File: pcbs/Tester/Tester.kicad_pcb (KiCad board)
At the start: 2 copper layers, 106 parts, among them J201 Raspberry_Pi_2_3, J301 Conn_02x20_Odd_Even, J401 Conn_02x20_Odd_Even, U201 SN74LVC4245APWR, U202 SN74LVC4245APWR, U203 SN74LVC4245APWR, U301 74HC595, U302 74HC595, U303 74HC595, U304 74HC595, U305 74HC595, U401 74HC165, U402 74HC165, U403 74HC165, U404 74HC165, U405 74HC165

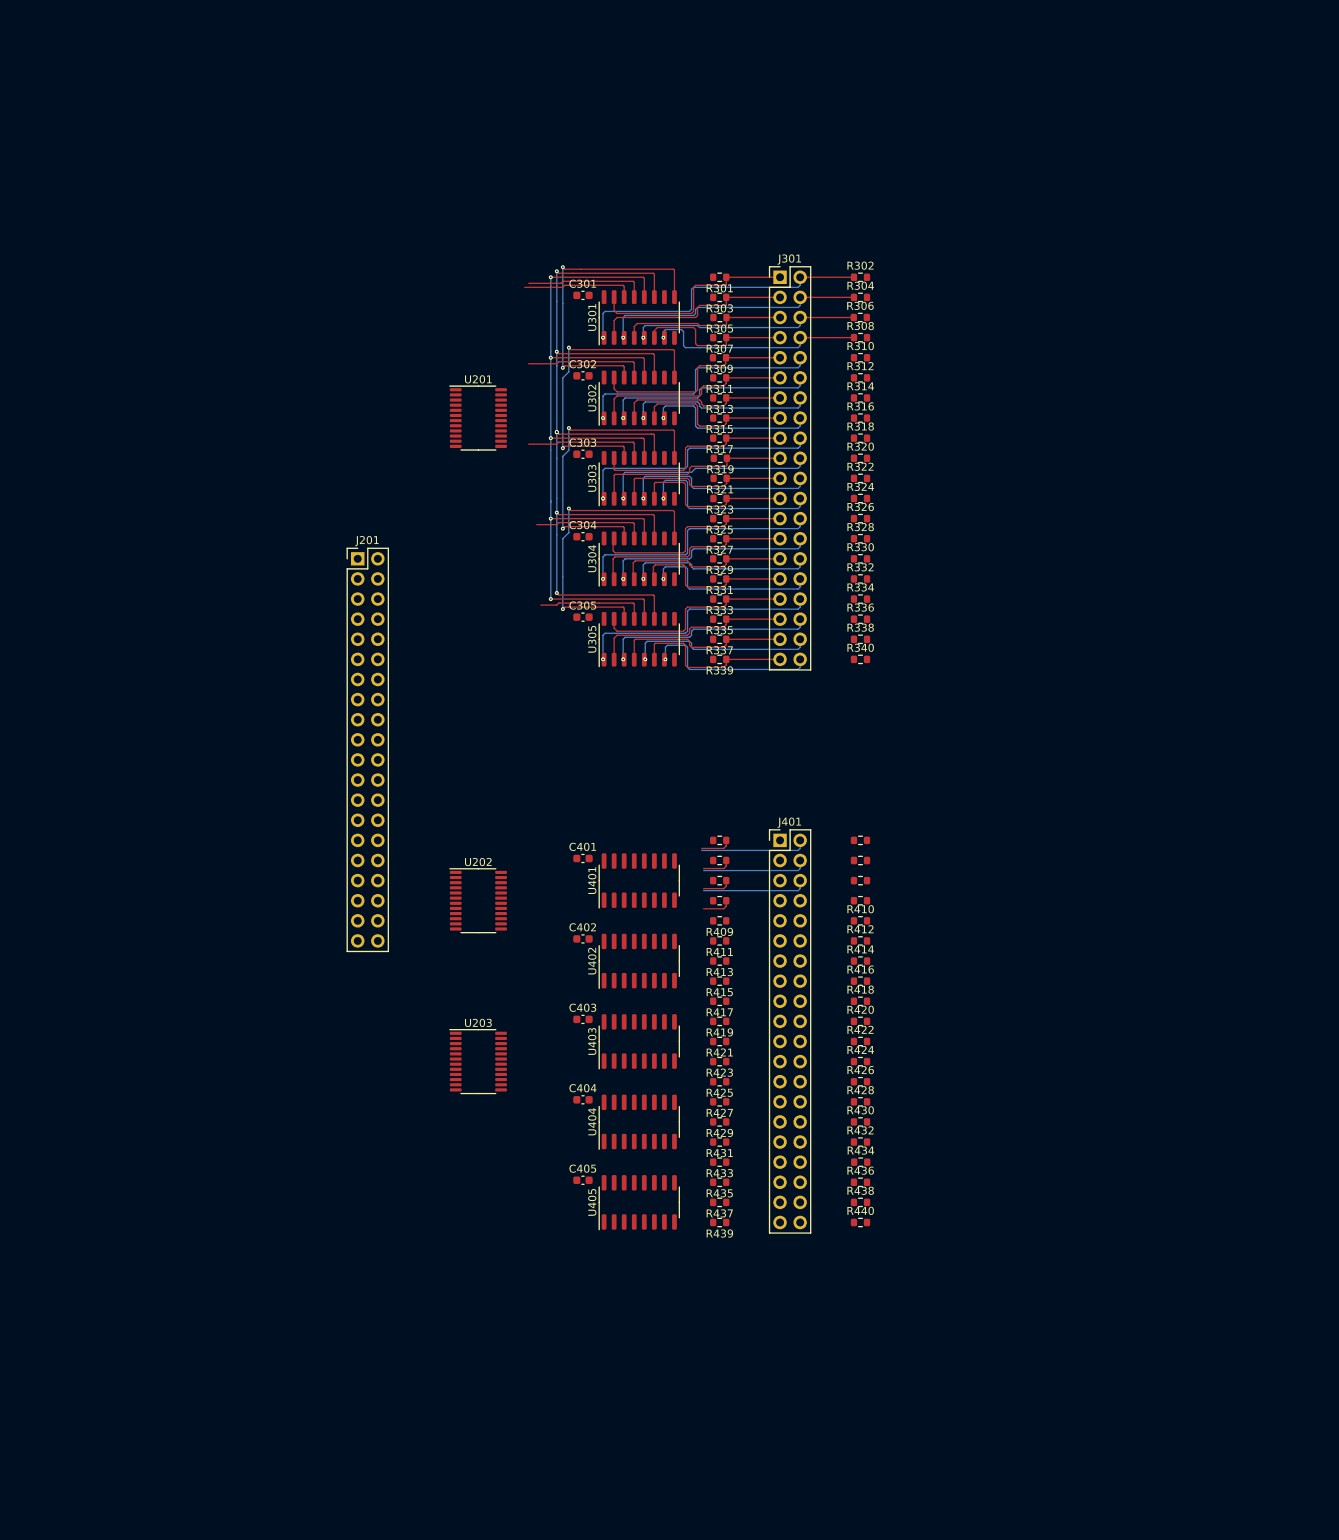
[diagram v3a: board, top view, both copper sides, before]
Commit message: Shift register routing
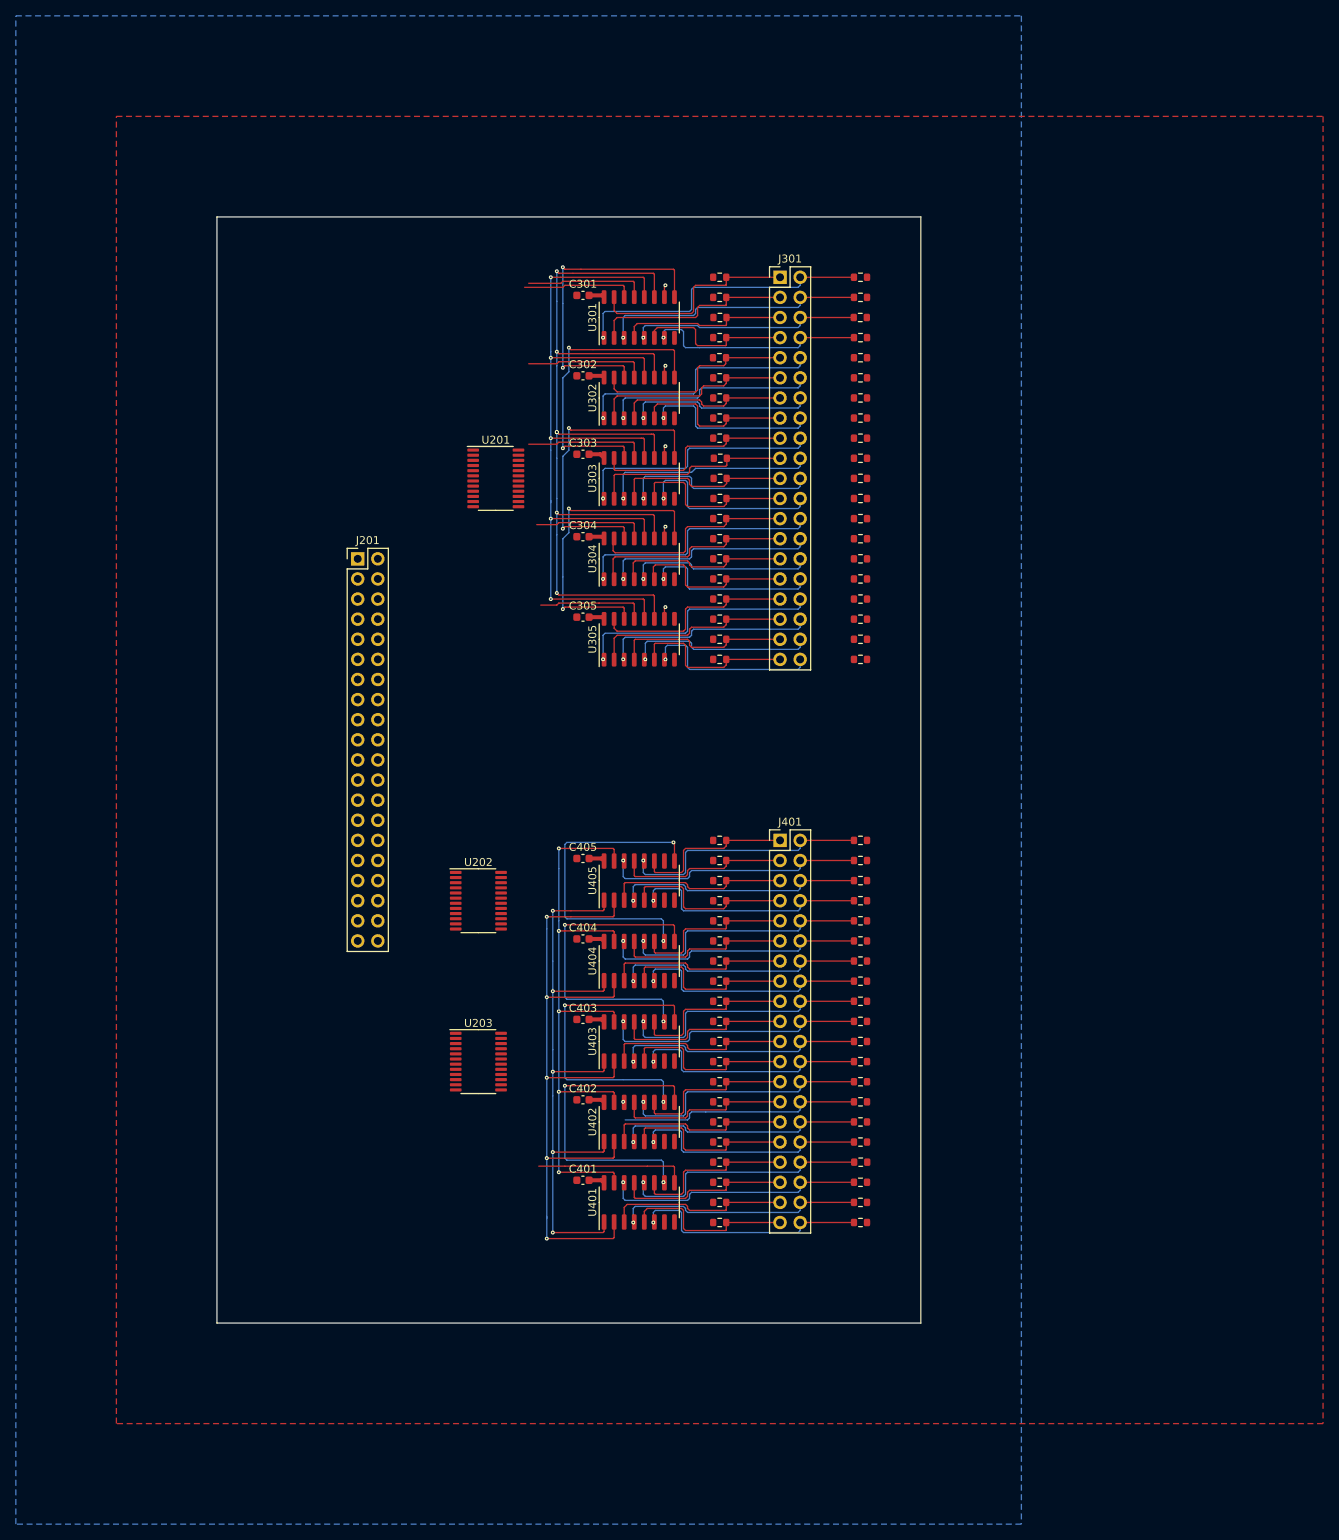
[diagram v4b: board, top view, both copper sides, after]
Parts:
- moved U401 40.6 mm to (129.5, 149.9)
- moved U405 40.6 mm to (129.5, 109.2)
- moved C401 40.6 mm to (122.4, 147.1)
- moved C405 40.6 mm to (122.4, 106.4)
- moved C402 20.3 mm to (122.4, 136.9)
- moved C404 20.3 mm to (122.4, 116.6)
- moved U402 20.3 mm to (129.5, 139.7)
- moved U404 20.3 mm to (129.5, 119.4)
- moved U201 7.93 mm to (111.4, 58.4)
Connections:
- U401 pad 11: /In Registers/In_{7} -> /In Registers/In_{32}
- U401 pad 12: /In Registers/In_{6} -> /In Registers/In_{33}
- U401 pad 13: /In Registers/In_{5} -> /In Registers/In_{34}
- U401 pad 14: /In Registers/In_{4} -> /In Registers/In_{35}
- U401 pad 3: /In Registers/In_{3} -> /In Registers/In_{36}
- U401 pad 4: /In Registers/In_{2} -> /In Registers/In_{37}
- U401 pad 5: /In Registers/In_{1} -> /In Registers/In_{38}
- U401 pad 6: /In Registers/In_{0} -> /In Registers/In_{39}
- U402 pad 11: unconnected-(U402-Pad11) -> /In Registers/In_{24}
- U402 pad 12: unconnected-(U402-Pad12) -> /In Registers/In_{25}
- U402 pad 13: unconnected-(U402-Pad13) -> /In Registers/In_{26}
- U402 pad 14: unconnected-(U402-Pad14) -> /In Registers/In_{27}
- U402 pad 3: unconnected-(U402-Pad3) -> /In Registers/In_{28}
- U402 pad 4: unconnected-(U402-Pad4) -> /In Registers/In_{29}
- U402 pad 5: unconnected-(U402-Pad5) -> /In Registers/In_{30}
- U402 pad 6: unconnected-(U402-Pad6) -> /In Registers/In_{31}
- U403 pad 11: unconnected-(U403-Pad11) -> /In Registers/In_{16}
- U403 pad 12: unconnected-(U403-Pad12) -> /In Registers/In_{17}
- U403 pad 13: unconnected-(U403-Pad13) -> /In Registers/In_{18}
- U403 pad 14: unconnected-(U403-Pad14) -> /In Registers/In_{19}
- U403 pad 3: unconnected-(U403-Pad3) -> /In Registers/In_{20}
- U403 pad 4: unconnected-(U403-Pad4) -> /In Registers/In_{21}
- U403 pad 5: unconnected-(U403-Pad5) -> /In Registers/In_{22}
- U403 pad 6: unconnected-(U403-Pad6) -> /In Registers/In_{23}
- U404 pad 11: unconnected-(U404-Pad11) -> /In Registers/In_{8}
- U404 pad 12: unconnected-(U404-Pad12) -> /In Registers/In_{9}
- U404 pad 13: unconnected-(U404-Pad13) -> /In Registers/In_{10}
- U404 pad 14: unconnected-(U404-Pad14) -> /In Registers/In_{11}
- U404 pad 3: unconnected-(U404-Pad3) -> /In Registers/In_{12}
- U404 pad 4: unconnected-(U404-Pad4) -> /In Registers/In_{13}
- U404 pad 5: unconnected-(U404-Pad5) -> /In Registers/In_{14}
- U404 pad 6: unconnected-(U404-Pad6) -> /In Registers/In_{15}
- U405 pad 11: unconnected-(U405-Pad11) -> /In Registers/In_{0}
- U405 pad 12: unconnected-(U405-Pad12) -> /In Registers/In_{1}
- U405 pad 13: unconnected-(U405-Pad13) -> /In Registers/In_{2}
- U405 pad 14: unconnected-(U405-Pad14) -> /In Registers/In_{3}
- U405 pad 3: unconnected-(U405-Pad3) -> /In Registers/In_{4}
- U405 pad 4: unconnected-(U405-Pad4) -> /In Registers/In_{5}
- U405 pad 5: unconnected-(U405-Pad5) -> /In Registers/In_{6}
- U405 pad 6: unconnected-(U405-Pad6) -> /In Registers/In_{7}
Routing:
- net /In Registers/IN_{CLK}: track 0.00 -> 93.6 mm, vias 0 -> 5
- net /In Registers/~{IN_{SELECT}}: track 0.00 -> 82.1 mm, vias 0 -> 5
- net /In Registers/~{IN_{LOAD}}: track 0.00 -> 79.3 mm, vias 0 -> 5
- net Net-(U404-Pad10): track 0.00 -> 40.6 mm, vias 0 -> 2
- net Net-(U401-Pad10): track 0.00 -> 40.2 mm, vias 0 -> 2
- net Net-(U403-Pad10): track 0.00 -> 40.2 mm, vias 0 -> 2
- net Net-(U402-Pad10): track 0.00 -> 40.2 mm, vias 0 -> 2
- net /In Registers/In_{19}: track 0.00 -> 33.6 mm, vias 0 -> 1
- net /In Registers/In_{35}: track 0.00 -> 33.1 mm, vias 0 -> 1
- net /In Registers/In_{11}: track 0.00 -> 33.1 mm, vias 0 -> 1
- net /In Registers/In_{17}: track 0.00 -> 32.6 mm, vias 0 -> 1
- net /In Registers/In_{33}: track 0.00 -> 32.1 mm, vias 0 -> 1
- net /In Registers/In_{9}: track 0.00 -> 32.1 mm, vias 0 -> 1
- net /In Registers/In_{25}: track 0.00 -> 32.1 mm, vias 0 -> 1
- net /In Registers/In_{29}: track 0.00 -> 31.3 mm, vias 0 -> 1
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- added copper zone on B.Cu, net +5V
- added copper zone on F.Cu, net /In Registers/In_{3}
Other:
- board outline added: 88.9 x 139.7 mm

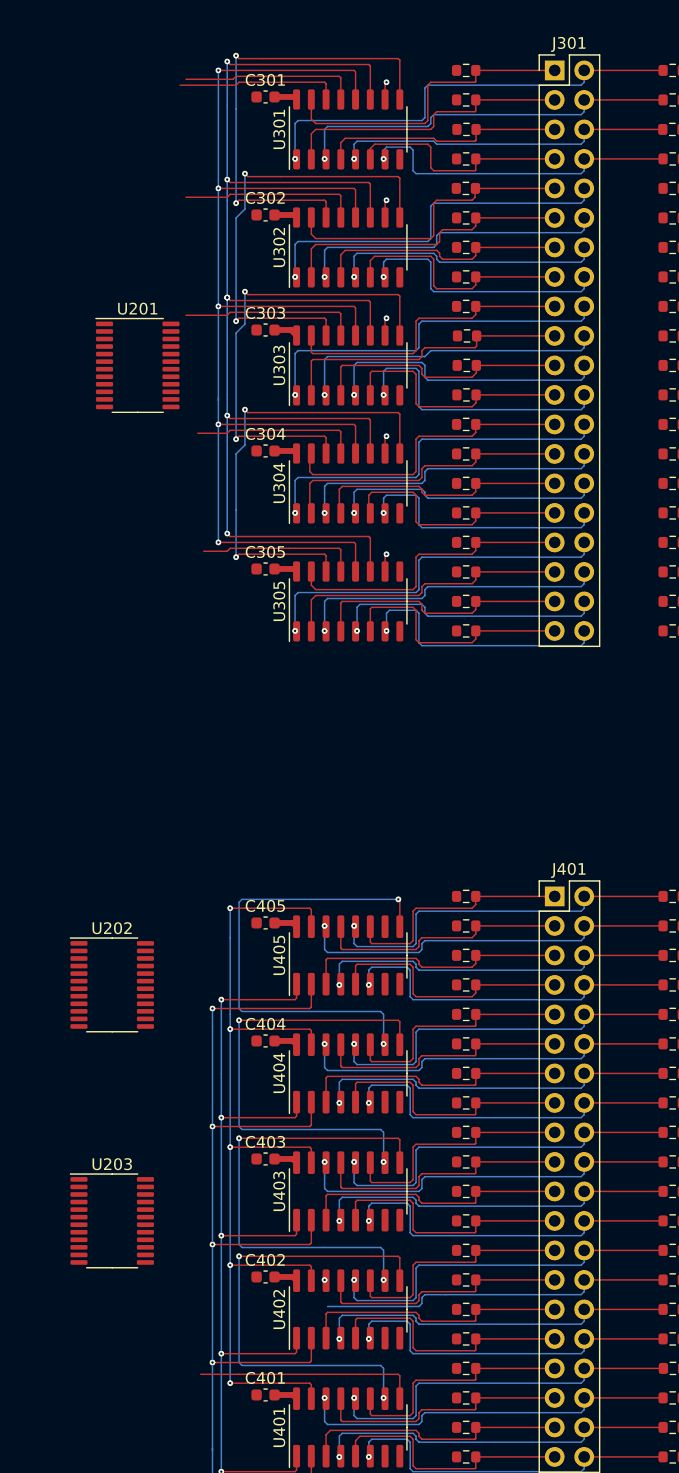
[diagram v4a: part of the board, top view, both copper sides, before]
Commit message: Turn those transceivers the other way up
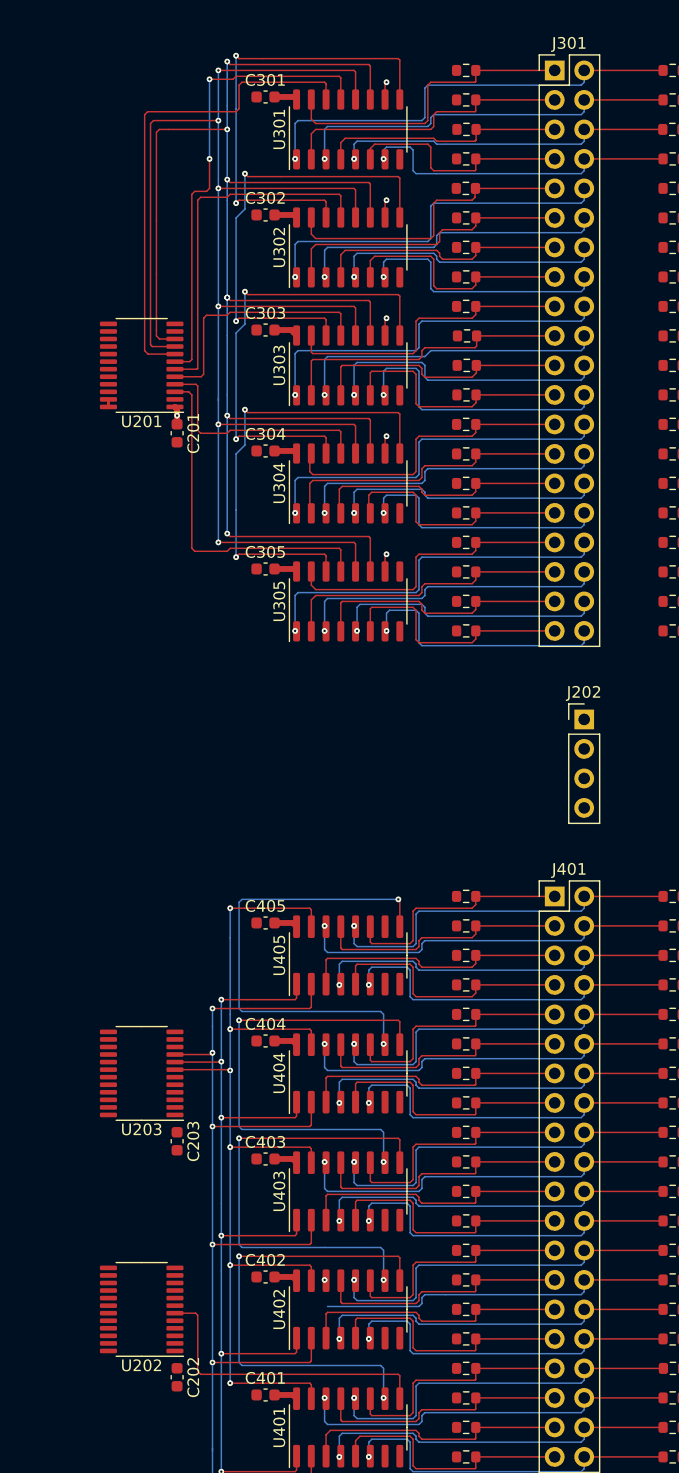
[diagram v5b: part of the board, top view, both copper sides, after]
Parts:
- added C201: 100n, Capacitor_SMD:C_0603_1608Metric, F.Cu at (114.8, 64.3)
- added C202: 100n, Capacitor_SMD:C_0603_1608Metric, F.Cu at (114.8, 145.5)
- added C203: 100n, Capacitor_SMD:C_0603_1608Metric, F.Cu at (114.8, 125.2)
- added J202: Conn_01x04, Connector_PinHeader_2.54mm:PinHeader_1x04_P2.54mm_Vertical, F.Cu at (149.9, 88.9)
- moved U202 28.1 mm to (111.8, 139.7), turned to 180 degrees
- moved U203 13.0 mm to (111.8, 119.4), turned to 180 degrees
- moved U201 0.34 mm to (111.8, 58.4), turned to 180 degrees
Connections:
- U201 pad 10: /Out Registers/~{OE5} -> /Out Registers/OUT_{CLK}
- U201 pad 14: /Pi Input/~{SPI0_{OE1}} -> /Pi Input/SPI0_{CLK}
- U201 pad 15: /Pi Input/~{SPI0_{OE1}} -> /Pi Input/~{SPI0_{SELECT}}
- U201 pad 16: /Pi Input/~{SPI0_{OE1}} -> /Pi Input/SPI0_{COPI}
- U201 pad 18: /Pi Input/~{SPI0_{OE1}} -> /Pi Input/~{SPI0_{OE2}}
- U201 pad 19: /Pi Input/SPI0_{CLK} -> /Pi Input/~{SPI0_{OE3}}
- U201 pad 20: /Pi Input/SPI0_{COPI} -> /Pi Input/~{SPI0_{OE4}}
- U201 pad 21: /Pi Input/~{SPI0_{SELECT}} -> /Pi Input/~{SPI0_{OE5}}
- U201 pad 3: /Out Registers/~{OUT_{SELECT}} -> /Out Registers/~{OE5}
- U201 pad 4: /Out Registers/OUT_{DATA} -> /Out Registers/~{OE4}
- U201 pad 5: /Out Registers/OUT_{CLK} -> /Out Registers/~{OE3}
- U201 pad 6: /Out Registers/~{OE1} -> /Out Registers/~{OE2}
- U201 pad 7: /Out Registers/~{OE2} -> /Out Registers/~{OE1}
- U201 pad 8: /Out Registers/~{OE3} -> /Out Registers/OUT_{DATA}
- U201 pad 9: /Out Registers/~{OE4} -> /Out Registers/~{OUT_{SELECT}}
- U202 pad 10: GND -> unconnected-(U202-Pad10)
- U202 pad 3: GND -> unconnected-(U202-Pad3)
- U202 pad 4: GND -> unconnected-(U202-Pad4)
- U202 pad 5: GND -> unconnected-(U202-Pad5)
- U202 pad 6: /Pi Input/IN_{DATA} -> /In Registers/IN_{DATA}
- U202 pad 7: GND -> unconnected-(U202-Pad7)
- U202 pad 8: GND -> unconnected-(U202-Pad8)
- U202 pad 9: GND -> unconnected-(U202-Pad9)
- U203 pad 14: GND -> unconnected-(U203-Pad14)
- U203 pad 18: GND -> unconnected-(U203-Pad18)
- U203 pad 7: /Pi Input/~{IN_{SELECT}} -> /In Registers/~{IN_{SELECT}}
- U203 pad 8: /Pi Input/~{IN_{LOAD}} -> /In Registers/~{IN_{LOAD}}
- U203 pad 9: /Pi Input/IN_{CLK} -> /In Registers/IN_{CLK}
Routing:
- net /Out Registers/OUT_{DATA}: track 14.1 -> 42.4 mm
- net /Out Registers/~{OUT_{SELECT}}: track 112.1 -> 139.3 mm, vias 5 -> 6
- net /Out Registers/OUT_{CLK}: track 117.5 -> 142.9 mm, vias 6 -> 7
- net /Out Registers/~{OE1}: track 15.4 -> 40.2 mm, vias 0 -> 2
- net /Out Registers/~{OE5}: track 13.8 -> 29.7 mm
- net /Out Registers/~{OE2}: track 15.4 -> 30.9 mm
- net /In Registers/IN_{DATA}: track 19.2 -> 26.4 mm
- net /Out Registers/~{OE3}: track 15.4 -> 21.3 mm
- net /Out Registers/~{OE4}: track 14.3 -> 20.3 mm
- net /In Registers/~{IN_{SELECT}}: track 82.1 -> 86.9 mm, vias 5 -> 6
- net /In Registers/~{IN_{LOAD}}: track 79.3 -> 83.3 mm, vias 5 -> 6
- net /In Registers/IN_{CLK}: track 93.6 -> 96.8 mm, vias 5 -> 6
- net +5V: track 27.8 -> 29.4 mm, vias 5 -> 6
- net +3V3: track 0.00 -> 0.65 mm
